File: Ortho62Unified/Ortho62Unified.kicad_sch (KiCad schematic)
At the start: 156 parts, among them J1 USB_B_Micro, SW1 SW_Push, SW10 SW_Push, SW11 SW_Push, SW12 SW_Push, SW13 SW_Push, SW14 SW_Push, SW15 SW_Push, SW16 SW_Push, SW17 SW_Push, SW18 SW_Push, SW19 SW_Push, SW2 SW_Push, SW20 SW_Push, SW21 SW_Push, SW22 SW_Push, SW23 SW_Push, SW24 SW_Push, SW25 SW_Push, SW26 SW_Push, SW27 SW_Push, SW28 SW_Push, SW29 SW_Push, SW3 SW_Push, SW30 SW_Push, SW31 SW_Push, SW32 SW_Push, SW33 SW_Push, SW34 SW_Push, SW35 SW_Push, SW36 SW_Push, SW37 SW_Push, SW38 SW_Push, SW39 SW_Push, SW4 SW_Push, SW40 SW_Push, SW41 SW_Push, SW42 SW_Push, SW43 SW_Push, SW44 SW_Push, SW45 SW_Push, SW46 SW_Push, SW47 SW_Push, SW48 SW_Push, SW49 SW_Push, SW5 SW_Push, SW50 SW_Push, SW51 SW_Push, SW52 SW_Push, SW53 SW_Push, SW54 SW_Push, SW55 SW_Push, SW56 SW_Push, SW57 SW_Push, SW58 SW_Push, SW59 SW_Push, SW6 SW_Push, SW60 SW_Push, SW61 SW_Push, SW62 SW_Push, SW63 SW_Push, SW64 SW_Push, SW65 SW_Push, SW66 SW_Push, SW7 SW_Push, SW8 SW_Push, SW9 SW_Push, U1 MCP1700T-3302E_TT, U2 RP2040

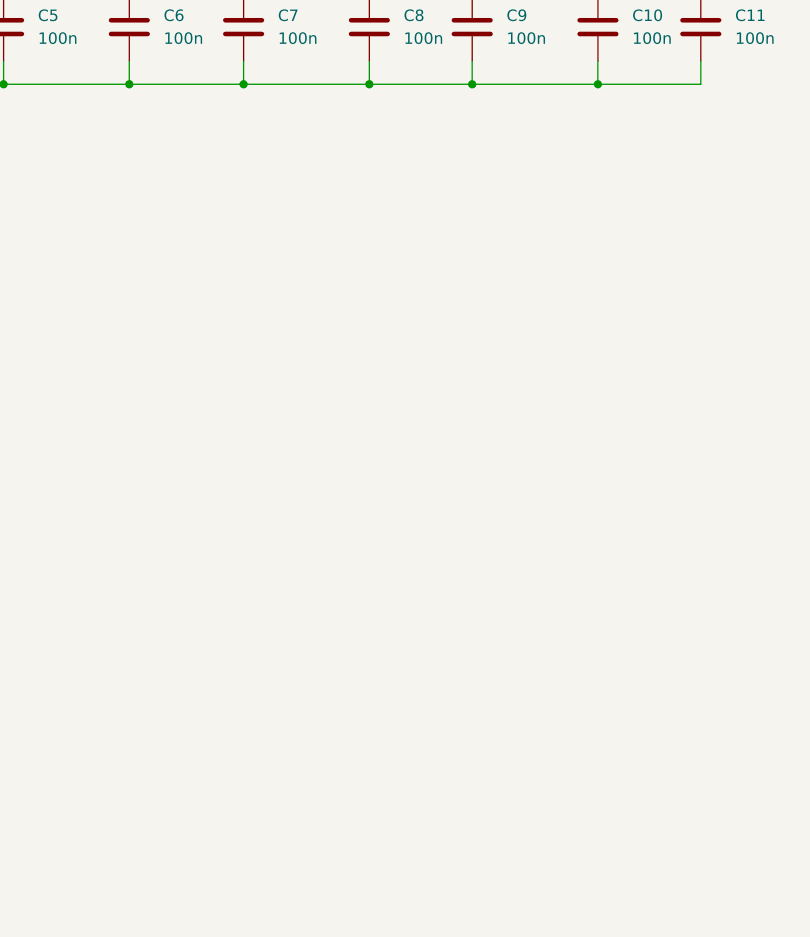
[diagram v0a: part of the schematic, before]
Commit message: Rearrange keys, add AVR micro.
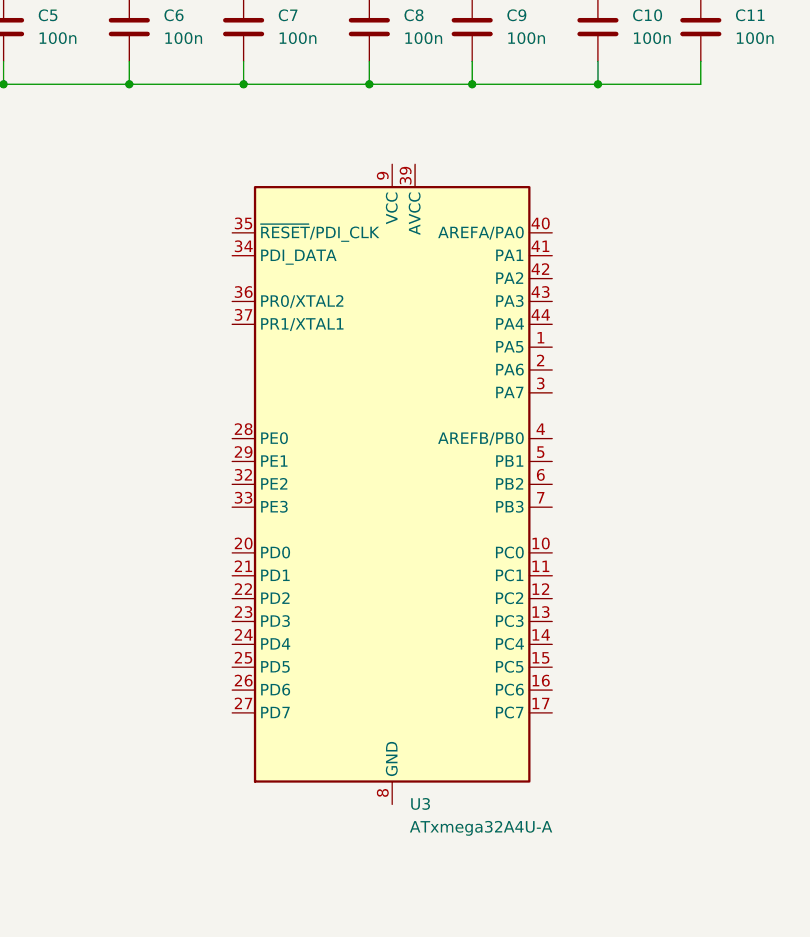
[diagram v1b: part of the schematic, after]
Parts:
- added U3: ATxmega32A4U-A, Package_QFP:TQFP-44_10x10mm_P0.8mm, symbol MCU_Microchip_ATmega:ATxmega32A4U-A
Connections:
- new net: U3.18 (GND), U3.30 (GND), U3.38 (GND), U3.8 (GND)
- new net: U3.19 (VCC), U3.31 (VCC), U3.9 (VCC)
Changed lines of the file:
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@@
+    )
+  )
+  (symbol (lib_id "MCU_Microchip_ATmega:ATxmega32A4U-A") (at 207.01 232.41 0) (unit 1)
+    (in_bom yes) (on_board yes) (dnp no) (fields_autoplaced)
+    (property "Reference" "U3" (at 208.9659 267.97 0)
+      (effects (font (size 1.27 1.27)) (justify left))
+    )
+    (property "Value" "ATxmega32A4U-A" (at 208.9659 270.51 0)
+      (effects (font (size 1.27 1.27)) (justify left))
+    )
+    (property "Footprint" "Package_QFP:TQFP-44_10x10mm_P0.8mm" (at 207.01 232.41 0)
+      (effects (font (size 1.27 1.27) italic) hide)
+    )
+    (property "Datasheet" "http://ww1.microchip.com/downloads/en/DeviceDoc/Atmel-8387-8-and16-bit-AVR-Microcontroller-XMEGA-A4U_Datasheet.pdf" (at 207.01 232.41 0)
+      (effects (font (size 1.27 1.27)) hide)
+    )
+    (pin "1")
+    (pin "10")
+    (pin "11")
+    (pin "12")
+    (pin "13")
+    (pin "14")
+    (pin "15")
+    (pin "16")
+    (pin "17")
+    (pin "18")
+    (pin "19")
+    (pin "2")
+    (pin "20")
+    (pin "21")
+    (pin "22")
+    (pin "23")
+    (pin "24")
+    (pin "25")
+    (pin "26")
+    (pin "27")
+    (pin "28")
+    (pin "29")
+    (pin "3")
+    (pin "30")
+    (pin "31")
+    (pin "32")
+    (pin "33")
+    (pin "34")
+    (pin "35")
+    (pin "36")
+    (pin "37")
+    (pin "38")
+    (pin "39")
+    (pin "4")
+    (pin "40")
+    (pin "41")
+    (pin "42")
+    (pin "43")
+    (pin "44")
+    (pin "5")
+    (pin "6")
+    (pin "7")
+    (pin "8")
+    (pin "9")
+    (instances
+      (project "Ortho62Unified"
+        (path "/439fef5a-3d16-441d-bc6a-72175770ebea"
+          (reference "U3") (unit 1)
+        )
+      )
     )
   )

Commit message: 66 symmetrical layout.
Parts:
- SW66: footprint Switch_Keyboard_Kailh:SW_Kailh_Choc_V1V2_1.00u -> Switch_Keyboard_Kailh:SW_Kailh_Choc_V1V2_1.50u
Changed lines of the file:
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@@
       (effects (font (size 1.27 1.27)))
     )
-    (property "Footprint" "Switch_Keyboard_Kailh:SW_Kailh_Choc_V1V2_1.00u" (at 276.225 137.795 0)
+    (property "Footprint" "Switch_Keyboard_Kailh:SW_Kailh_Choc_V1V2_1.50u" (at 276.225 137.795 0)
       (effects (font (size 1.27 1.27)) hide)
     )

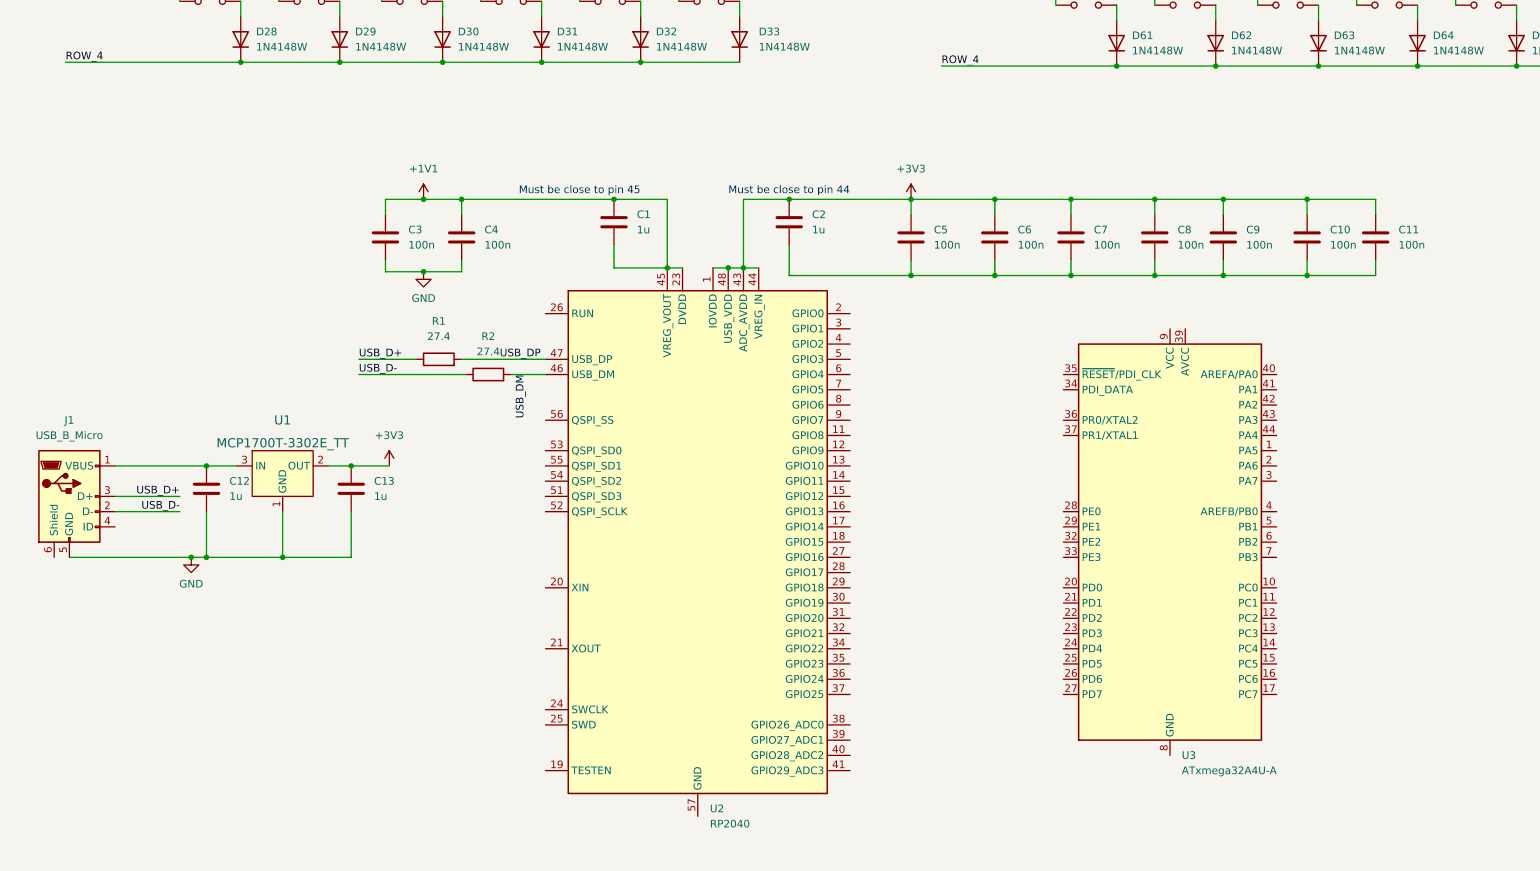
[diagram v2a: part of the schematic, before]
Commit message: Align and correctly space 66 keys.
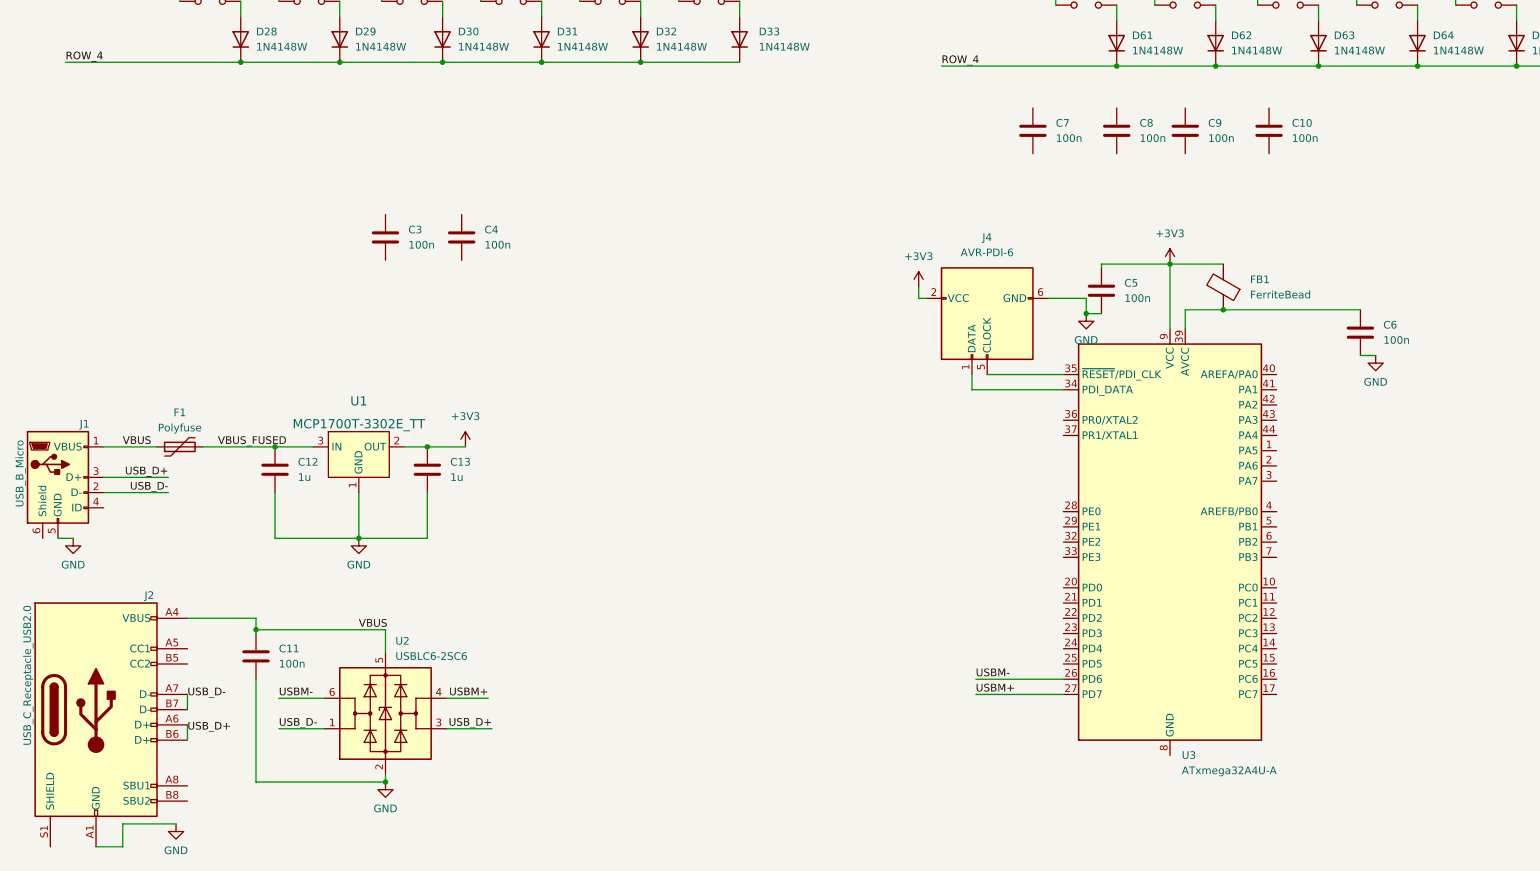
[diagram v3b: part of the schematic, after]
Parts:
- removed C1, C2: 1u, Capacitor_SMD:C_0603_1608Metric, symbol Device:C
- removed R1, R2: 27.4, Resistor_SMD:R_0603_1608Metric, symbol Device:R
- removed U2: RP2040, Package_DFN_QFN:QFN-56-1EP_7x7mm_P0.4mm_EP3.2x3.2mm, symbol MCU_RaspberryPi:RP2040
- added F1: Polyfuse, Fuse:Fuse_1206_3216Metric_Pad1.42x1.75mm_HandSolder, symbol Device:Polyfuse
- added FB1: FerriteBead, Fuse:Fuse_0603_1608Metric_Pad1.05x0.95mm_HandSolder, symbol Device:FerriteBead
- added J2: USB_C_Receptacle_USB2.0, symbol Connector:USB_C_Receptacle_USB2.0
- added J4: AVR-PDI-6, symbol Connector:AVR-PDI-6
- added U2: USBLC6-2SC6, Package_TO_SOT_SMD:SOT-23-6, symbol Power_Protection:USBLC6-2SC6
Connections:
- net +3V3: now also U3.19 (VCC), U3.31 (VCC), U3.9 (VCC), FB1.2, J4.2 (VCC); no longer C10.1, C11.1, C6.1, C7.1, C8.1, C9.1
- net GND: now also C11.2, C5.2, C6.2, J2.A1 (GND), J2.A12 (GND), J2.B1 (GND), J2.B12 (GND), J4.6 (GND), U2.2 (GND); no longer C3.2, C4.2
- net USB_D+: now also J2.A6 (D+), J2.B6 (D+), U2.3 (I/O2)
- net USB_D-: now also J2.A7 (D-), J2.B7 (D-), U2.1 (I/O1)
- net USBM-: now reaches U3.26 (PD6)
- net USBM-: now also U2.6 (I/O1)
- net USBM+: now reaches U3.27 (PD7)
- net USBM+: now also U2.4 (I/O2)
- net at U3.34 (PDI_DATA): now also J4.1 (DATA)
- net at U3.35 (~{RESET}/PDI_CLK): now also J4.5 (CLOCK)
- net at U3.39 (AVCC): now also C6.1, FB1.1
- net VBUS_FUSED: now reaches C12.1, U1.3 (IN)
- net VBUS_FUSED: now also F1.2; no longer J1.1 (VBUS)
- net +1V1: no longer names the net of C4.1
- net +1V1: no longer C3.1
- new net VBUS: C11.1, F1.1, J1.1 (VBUS), J2.A4 (VBUS), J2.A9 (VBUS), J2.B4 (VBUS), J2.B9 (VBUS), U2.5 (VBUS)
- now unconnected: C10.2, C7.2, C8.2, C9.2
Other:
- note removed: "Must be close to pin 44"
- note removed: "Must be close to pin 45"
- moved on the sheet: C10, C11, C13, C5, C6, C7, C8, C9, J1, U1

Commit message: Add function keys row.
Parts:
- removed C10, C3, C4, C7, C8, C9: 100n, Capacitor_SMD:C_0603_1608Metric, symbol Device:C
- removed J1: USB_B_Micro, Connector_USB:USB_Micro-B_Molex_47346-0001, symbol Connector:USB_B_Micro
- added D55, D68, D69, D70, D71, D72, D73, D74, D75, D76, D77, D78, D79, D80, D81, D82: 1N4148W, Diode_SMD:D_SOD-123, symbol Diode:1N4148W
- added SW55, SW68, SW69, SW70, SW71, SW72, SW73, SW74, SW76, SW77, SW78, SW79, SW80, SW81: SW_Push, Switch_Keyboard_Kailh:SW_Kailh_Choc_V1V2_1.00u, symbol Switch:SW_Push
- added SW75, SW82: SW_Push, Switch_Keyboard_Kailh:SW_Kailh_Choc_V1V2_1.50u, symbol Switch:SW_Push
- C1: renamed from C5; value 100n -> C; footprint Capacitor_SMD:C_0603_1608Metric -> Capacitor_SMD:C_0603_1608Metric_Pad1.08x0.95mm_HandSolder
- C2: renamed from C6; value 100n -> C; footprint Capacitor_SMD:C_0603_1608Metric -> Capacitor_SMD:C_0603_1608Metric_Pad1.08x0.95mm_HandSolder
- C3: renamed from C12; value 1u -> C; footprint Capacitor_SMD:C_0603_1608Metric -> Capacitor_SMD:C_0603_1608Metric_Pad1.08x0.95mm_HandSolder
- C4: renamed from C13; value 1u -> C; footprint Capacitor_SMD:C_0603_1608Metric -> Capacitor_SMD:C_0603_1608Metric_Pad1.08x0.95mm_HandSolder
- C5: renamed from C11; value 100n -> C; footprint Capacitor_SMD:C_0603_1608Metric -> Capacitor_SMD:C_0603_1608Metric_Pad1.08x0.95mm_HandSolder
- D1, D2, D3, D4, D5, D6, D7: footprint Diode_SMD:D_SOD-323_Hand_Split_Keyboard -> Diode_SMD:D_SOD-123
- D10: renamed from D36; footprint Diode_SMD:D_SOD-323_Hand_Split_Keyboard -> Diode_SMD:D_SOD-123
- D11: renamed from D37; footprint Diode_SMD:D_SOD-323_Hand_Split_Keyboard -> Diode_SMD:D_SOD-123
- D12: renamed from D38; footprint Diode_SMD:D_SOD-323_Hand_Split_Keyboard -> Diode_SMD:D_SOD-123
- D13: renamed from D39; footprint Diode_SMD:D_SOD-323_Hand_Split_Keyboard -> Diode_SMD:D_SOD-123
- D14: renamed from D40; footprint Diode_SMD:D_SOD-323_Hand_Split_Keyboard -> Diode_SMD:D_SOD-123
- D15: renamed from D10; footprint Diode_SMD:D_SOD-323_Hand_Split_Keyboard -> Diode_SMD:D_SOD-123
- D16: renamed from D11; footprint Diode_SMD:D_SOD-323_Hand_Split_Keyboard -> Diode_SMD:D_SOD-123
- D17: renamed from D12; footprint Diode_SMD:D_SOD-323_Hand_Split_Keyboard -> Diode_SMD:D_SOD-123
- D18: renamed from D13; footprint Diode_SMD:D_SOD-323_Hand_Split_Keyboard -> Diode_SMD:D_SOD-123
- D19: renamed from D14; footprint Diode_SMD:D_SOD-323_Hand_Split_Keyboard -> Diode_SMD:D_SOD-123
- D20: renamed from D15; footprint Diode_SMD:D_SOD-323_Hand_Split_Keyboard -> Diode_SMD:D_SOD-123
- D21: renamed from D8; footprint Diode_SMD:D_SOD-323_Hand_Split_Keyboard -> Diode_SMD:D_SOD-123
- D22: renamed from D41; footprint Diode_SMD:D_SOD-323_Hand_Split_Keyboard -> Diode_SMD:D_SOD-123
- D23: renamed from D42; footprint Diode_SMD:D_SOD-323_Hand_Split_Keyboard -> Diode_SMD:D_SOD-123
- D24: renamed from D43; footprint Diode_SMD:D_SOD-323_Hand_Split_Keyboard -> Diode_SMD:D_SOD-123
- D25: renamed from D44; footprint Diode_SMD:D_SOD-323_Hand_Split_Keyboard -> Diode_SMD:D_SOD-123
- D26: renamed from D45; footprint Diode_SMD:D_SOD-323_Hand_Split_Keyboard -> Diode_SMD:D_SOD-123
- D27: renamed from D46; footprint Diode_SMD:D_SOD-323_Hand_Split_Keyboard -> Diode_SMD:D_SOD-123
- D28: renamed from D47; footprint Diode_SMD:D_SOD-323_Hand_Split_Keyboard -> Diode_SMD:D_SOD-123
- D29: renamed from D16; footprint Diode_SMD:D_SOD-323_Hand_Split_Keyboard -> Diode_SMD:D_SOD-123
- D30: renamed from D17; footprint Diode_SMD:D_SOD-323_Hand_Split_Keyboard -> Diode_SMD:D_SOD-123
- D31: renamed from D18; footprint Diode_SMD:D_SOD-323_Hand_Split_Keyboard -> Diode_SMD:D_SOD-123
- D32: renamed from D19; footprint Diode_SMD:D_SOD-323_Hand_Split_Keyboard -> Diode_SMD:D_SOD-123
- D33: renamed from D20; footprint Diode_SMD:D_SOD-323_Hand_Split_Keyboard -> Diode_SMD:D_SOD-123
- D34: renamed from D21; footprint Diode_SMD:D_SOD-323_Hand_Split_Keyboard -> Diode_SMD:D_SOD-123
- D35: renamed from D9; footprint Diode_SMD:D_SOD-323_Hand_Split_Keyboard -> Diode_SMD:D_SOD-123
- D36: renamed from D48; footprint Diode_SMD:D_SOD-323_Hand_Split_Keyboard -> Diode_SMD:D_SOD-123
- D37: renamed from D49; footprint Diode_SMD:D_SOD-323_Hand_Split_Keyboard -> Diode_SMD:D_SOD-123
- D38: renamed from D50; footprint Diode_SMD:D_SOD-323_Hand_Split_Keyboard -> Diode_SMD:D_SOD-123
- D39: renamed from D51; footprint Diode_SMD:D_SOD-323_Hand_Split_Keyboard -> Diode_SMD:D_SOD-123
- D40: renamed from D52; footprint Diode_SMD:D_SOD-323_Hand_Split_Keyboard -> Diode_SMD:D_SOD-123
- D41: renamed from D53; footprint Diode_SMD:D_SOD-323_Hand_Split_Keyboard -> Diode_SMD:D_SOD-123
- D42: renamed from D54; footprint Diode_SMD:D_SOD-323_Hand_Split_Keyboard -> Diode_SMD:D_SOD-123
- D43: renamed from D22; footprint Diode_SMD:D_SOD-323_Hand_Split_Keyboard -> Diode_SMD:D_SOD-123
- D44: renamed from D23; footprint Diode_SMD:D_SOD-323_Hand_Split_Keyboard -> Diode_SMD:D_SOD-123
- D45: renamed from D24; footprint Diode_SMD:D_SOD-323_Hand_Split_Keyboard -> Diode_SMD:D_SOD-123
- D46: renamed from D25; footprint Diode_SMD:D_SOD-323_Hand_Split_Keyboard -> Diode_SMD:D_SOD-123
- D47: renamed from D26; footprint Diode_SMD:D_SOD-323_Hand_Split_Keyboard -> Diode_SMD:D_SOD-123
- D48: renamed from D27; footprint Diode_SMD:D_SOD-323_Hand_Split_Keyboard -> Diode_SMD:D_SOD-123
- D49: renamed from D55; footprint Diode_SMD:D_SOD-323_Hand_Split_Keyboard -> Diode_SMD:D_SOD-123
- D50: renamed from D56; footprint Diode_SMD:D_SOD-323_Hand_Split_Keyboard -> Diode_SMD:D_SOD-123
- D51: renamed from D57; footprint Diode_SMD:D_SOD-323_Hand_Split_Keyboard -> Diode_SMD:D_SOD-123
- D52: renamed from D58; footprint Diode_SMD:D_SOD-323_Hand_Split_Keyboard -> Diode_SMD:D_SOD-123
- D53: renamed from D59; footprint Diode_SMD:D_SOD-323_Hand_Split_Keyboard -> Diode_SMD:D_SOD-123
- D54: renamed from D60; footprint Diode_SMD:D_SOD-323_Hand_Split_Keyboard -> Diode_SMD:D_SOD-123
- D56: renamed from D28; footprint Diode_SMD:D_SOD-323_Hand_Split_Keyboard -> Diode_SMD:D_SOD-123
- D57: renamed from D29; footprint Diode_SMD:D_SOD-323_Hand_Split_Keyboard -> Diode_SMD:D_SOD-123
- D58: renamed from D30; footprint Diode_SMD:D_SOD-323_Hand_Split_Keyboard -> Diode_SMD:D_SOD-123
- D59: renamed from D31; footprint Diode_SMD:D_SOD-323_Hand_Split_Keyboard -> Diode_SMD:D_SOD-123
- D60: renamed from D32; footprint Diode_SMD:D_SOD-323_Hand_Split_Keyboard -> Diode_SMD:D_SOD-123
- D61: renamed from D33; footprint Diode_SMD:D_SOD-323_Hand_Split_Keyboard -> Diode_SMD:D_SOD-123
- D62: renamed from D61; footprint Diode_SMD:D_SOD-323_Hand_Split_Keyboard -> Diode_SMD:D_SOD-123
- D63: renamed from D62; footprint Diode_SMD:D_SOD-323_Hand_Split_Keyboard -> Diode_SMD:D_SOD-123
- D64: renamed from D63; footprint Diode_SMD:D_SOD-323_Hand_Split_Keyboard -> Diode_SMD:D_SOD-123
- D65: renamed from D64; footprint Diode_SMD:D_SOD-323_Hand_Split_Keyboard -> Diode_SMD:D_SOD-123
- D66: renamed from D65; footprint Diode_SMD:D_SOD-323_Hand_Split_Keyboard -> Diode_SMD:D_SOD-123
- D67: renamed from D66; footprint Diode_SMD:D_SOD-323_Hand_Split_Keyboard -> Diode_SMD:D_SOD-123
- D8: renamed from D34; footprint Diode_SMD:D_SOD-323_Hand_Split_Keyboard -> Diode_SMD:D_SOD-123
- D9: renamed from D35; footprint Diode_SMD:D_SOD-323_Hand_Split_Keyboard -> Diode_SMD:D_SOD-123
- FB1: footprint Fuse:Fuse_0603_1608Metric_Pad1.05x0.95mm_HandSolder -> Inductor_SMD:L_0603_1608Metric_Pad1.05x0.95mm_HandSolder
- J1: renamed from J4; footprint (none) -> Connector_PinHeader_2.54mm:PinHeader_2x03_P2.54mm_Horizontal
- J3: renamed from J2; footprint (none) -> CustomHandSolderConnectors:USB_C_Receptacle_GCT_USB4085_HandSolder_SMT
- SW57: renamed from SW26; footprint Switch_Keyboard_Kailh:SW_Kailh_Choc_V1V2_1.00u -> Switch_Keyboard_Kailh:SW_Kailh_Choc_V1V2_1.50u
- SW58: renamed from SW27; footprint Switch_Keyboard_Kailh:SW_Kailh_Choc_V1V2_1.00u -> Switch_Keyboard_Kailh:SW_Kailh_Choc_V1V2_1.50u
- renumbered H2 to H1, H3 to H2, H4 to H3, H5 to H4, H6 to H5, H7 to H6, SW36 to SW10, SW37 to SW11, SW38 to SW12, SW39 to SW13, SW40 to SW14, SW7 to SW15, SW8 to SW16, SW9 to SW17, SW10 to SW18, SW11 to SW19, SW12 to SW20, SW32 to SW21, SW41 to SW22, SW42 to SW23, SW43 to SW24, SW44 to SW25, SW45 to SW26, SW46 to SW27, SW47 to SW28, SW13 to SW29, SW14 to SW30, SW15 to SW31, SW16 to SW32, SW17 to SW33, SW18 to SW34, SW33 to SW35, SW48 to SW36, SW49 to SW37, SW50 to SW38, SW51 to SW39, SW52 to SW40, SW53 to SW41, SW54 to SW42, SW19 to SW43, SW20 to SW44, SW21 to SW45, SW22 to SW46, SW23 to SW47, SW24 to SW48, SW55 to SW49, SW56 to SW50, SW57 to SW51, SW58 to SW52, SW59 to SW53, SW60 to SW54, SW25 to SW56, SW28 to SW59, SW29 to SW60, SW30 to SW61, SW61 to SW62, SW62 to SW63, SW63 to SW64, SW64 to SW65, SW65 to SW66, SW66 to SW67, SW31 to SW7, SW34 to SW8, SW35 to SW9, U3 to U2, U2 to U3
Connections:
- net COL_0: now also SW69.1
- net COL_1: now also SW70.1
- net COL_10: now also SW79.1
- net COL_11: now also SW80.1
- net COL_12: now also SW81.1
- net COL_13: now also SW55.1, SW68.1, SW82.1
- net COL_2: now also SW71.1
- net COL_3: now also SW72.1
- net COL_4: now also SW73.1
- net COL_5: now also SW74.1
- net COL_6: now also SW75.1
- net COL_7: now also SW76.1
- net COL_8: now also SW77.1
- net COL_9: now also SW78.1
- net GND: now also U2.18 (GND), U2.30 (GND), U2.38 (GND), U2.8 (GND)
- net ROW_0: now also D76.1 (K), D77.1 (K), D78.1 (K), D79.1 (K), D80.1 (K), D81.1 (K), D82.1 (K)
- net ROW_3: now also D55.1 (K)
- net ROW_4: now also D68.1 (K)
- new net: D79.2 (A), SW79.2
- new net: D74.2 (A), SW74.2
- new net: D75.2 (A), SW75.2
- new net: D76.2 (A), SW76.2
- new net: D68.2 (A), SW68.2
- new net: D73.2 (A), SW73.2
- new net: D82.2 (A), SW82.2
- new net: D55.2 (A), SW55.2
- new net: D70.2 (A), SW70.2
- new net: D81.2 (A), SW81.2
- new net: D77.2 (A), SW77.2
- new net: D80.2 (A), SW80.2
- new net: D71.2 (A), SW71.2
- new net: D72.2 (A), SW72.2
- new net: D78.2 (A), SW78.2
- new net: D69.2 (A), SW69.2
- new net ROW_F: D69.1 (K), D70.1 (K), D71.1 (K), D72.1 (K), D73.1 (K), D74.1 (K), D75.1 (K)
- no-connect marks 0 -> 4
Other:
- moved on the sheet: C1, C2, C3, C4, C5, D1, D10, D11, D12, D13, D14, D15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

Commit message: Place and align all 82 keys.
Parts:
- SW57, SW58: footprint Switch_Keyboard_Kailh:SW_Kailh_Choc_V1V2_1.50u -> Switch_Keyboard_Kailh:SW_Kailh_Choc_V1V2_1.00u
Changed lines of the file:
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@@
       (effects (font (size 1.27 1.27)))
     )
-    (property "Footprint" "Switch_Keyboard_Kailh:SW_Kailh_Choc_V1V2_1.50u" (at 63.5 137.16 0)
+    (property "Footprint" "Switch_Keyboard_Kailh:SW_Kailh_Choc_V1V2_1.00u" (at 63.5 137.16 0)
       (effects (font (size 1.27 1.27)) hide)
     )
@@
       (effects (font (size 1.27 1.27)))
     )
-    (property "Footprint" "Switch_Keyboard_Kailh:SW_Kailh_Choc_V1V2_1.50u" (at 81.28 137.16 0)
-      (effects (font (size 1.27 1.27)) hide)
-    )
+    (property "Footprint" "Switch_Keyboard_Kailh:SW_Kailh_Choc_V1V2_1.00u" (at 81.28 137.16 0)
+      (effects (font (size 1.27 1.27)) hide)
+    )
